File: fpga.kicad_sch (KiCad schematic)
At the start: 62 parts, among them CON1 SD_Card_DM3BT, P10 CONN_01X01, P11 CONN_01X01, P12 CONN_01X01, P13 CONN_01X01, P14 CONN_01X01, P15 CONN_01X01, P16 CONN_01X01, P3 CONN_02X04, P4 CONN_02X04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

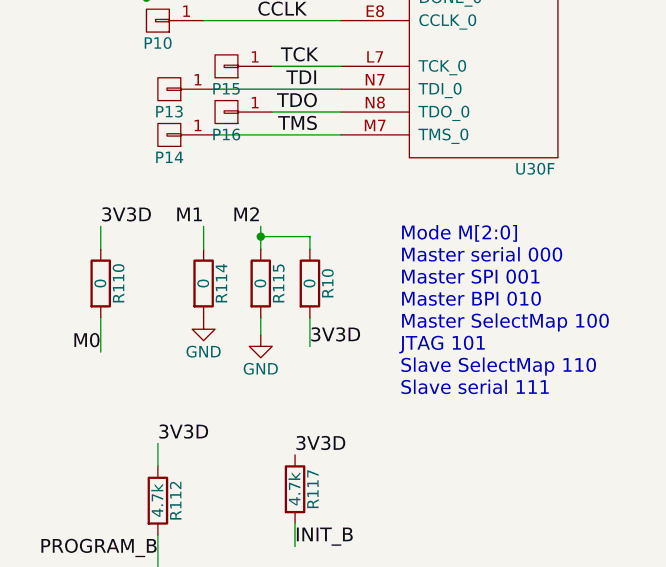
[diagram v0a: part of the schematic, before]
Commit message: Artix 7 Mode pin 2 was connected to 3.3 and Gnd. It is corrected. It is in JTAG mode for now. I will add dip switch
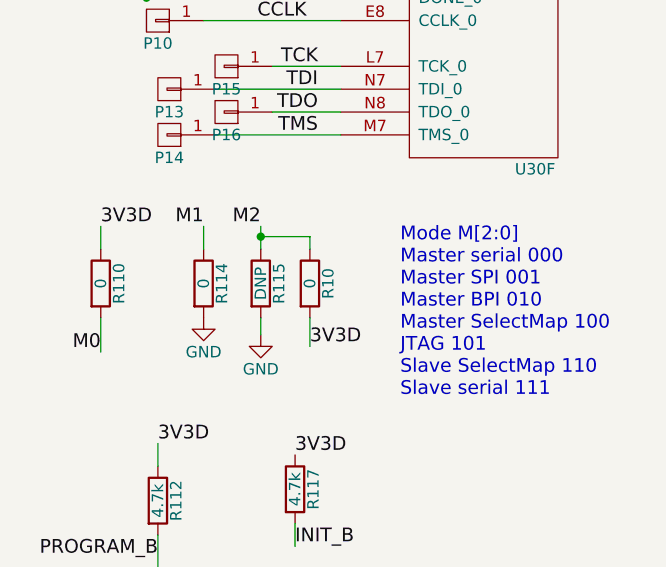
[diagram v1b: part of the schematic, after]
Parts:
- R115: value 0 -> DNP
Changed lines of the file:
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@@
 			)
 		)
-		(property "Value" "0"
+		(property "Value" "DNP"
 			(at 36.83 182.88 90)
 			(effects

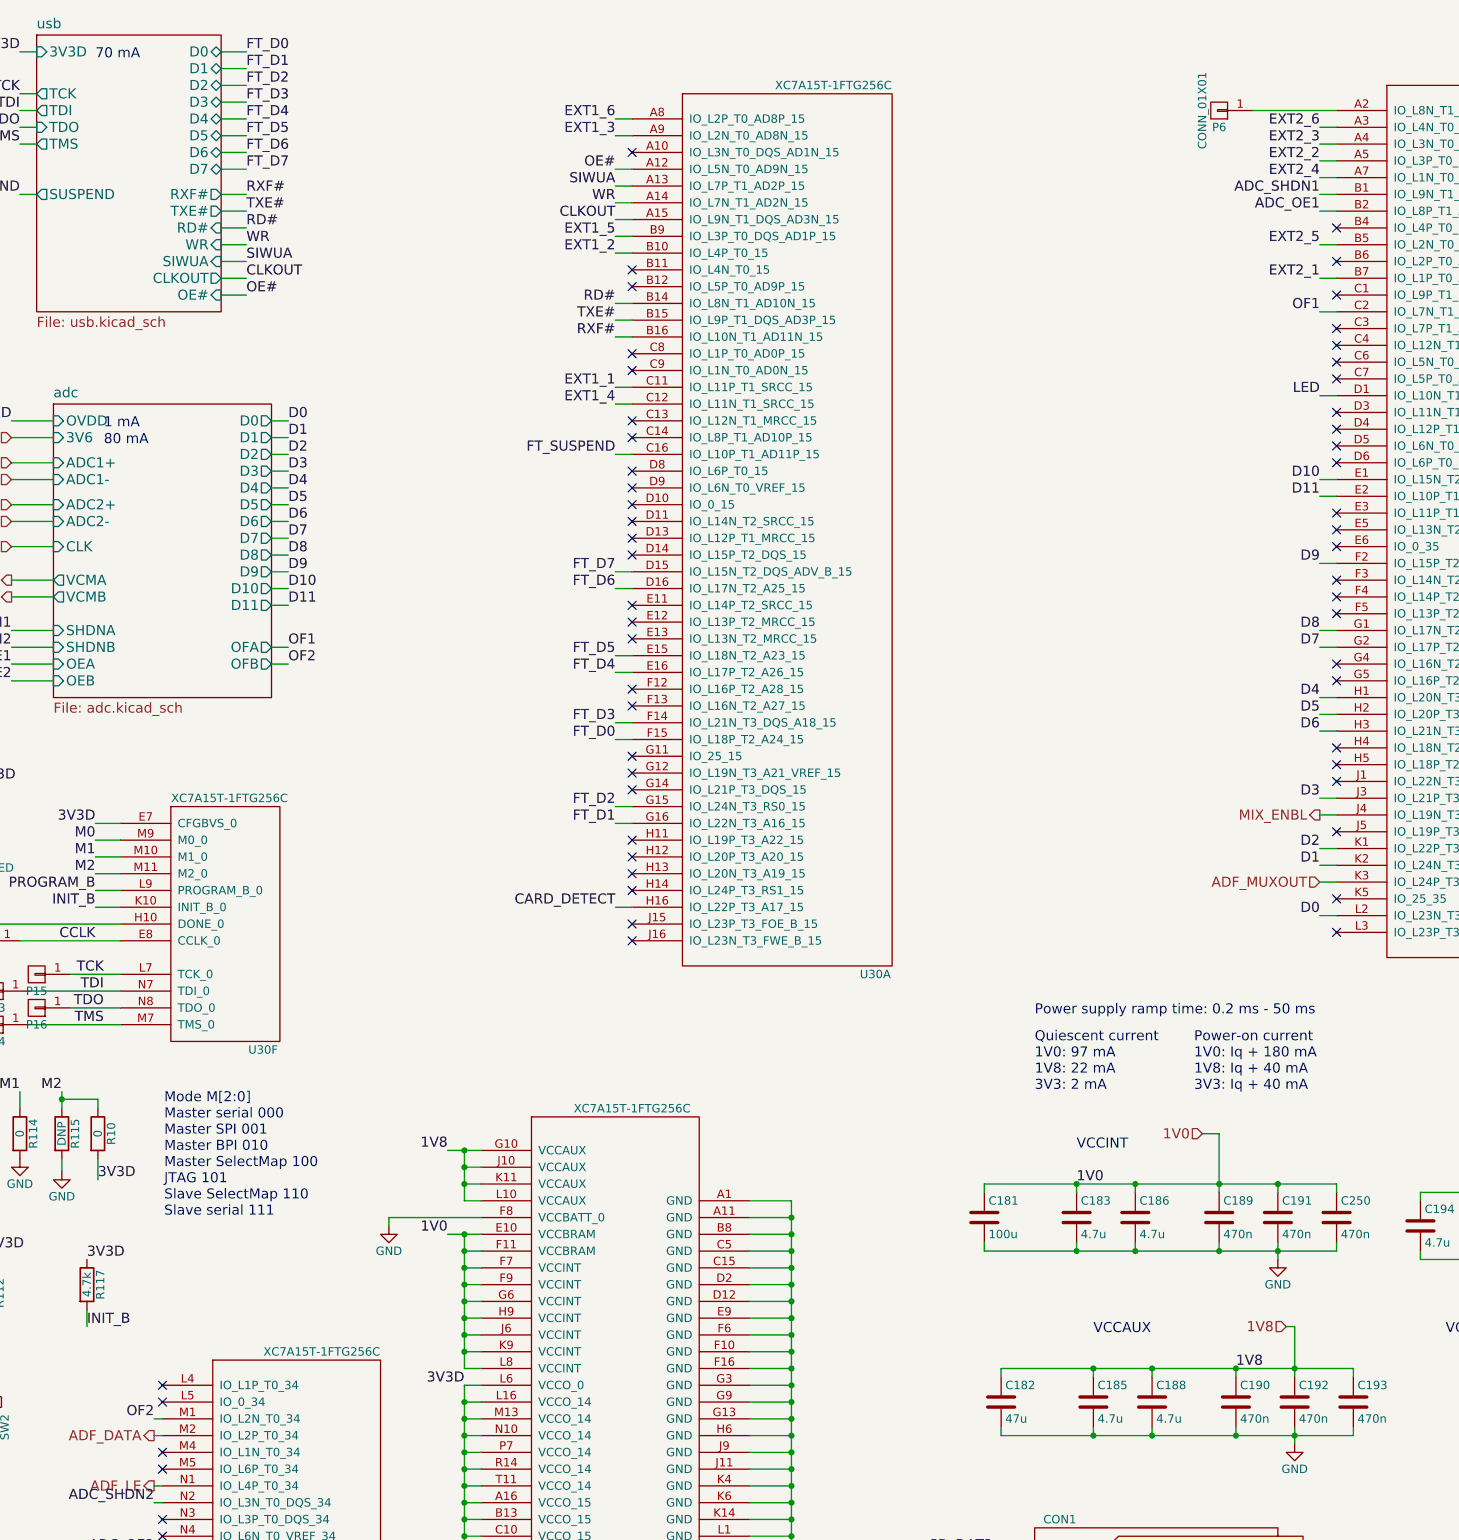
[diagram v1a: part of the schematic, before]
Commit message: Reset button is added. Detout is connected to an adc pin of fpga. Unused pad is deleted. Pins are check. Notes are added on pcb side. No problem related error drc excluded
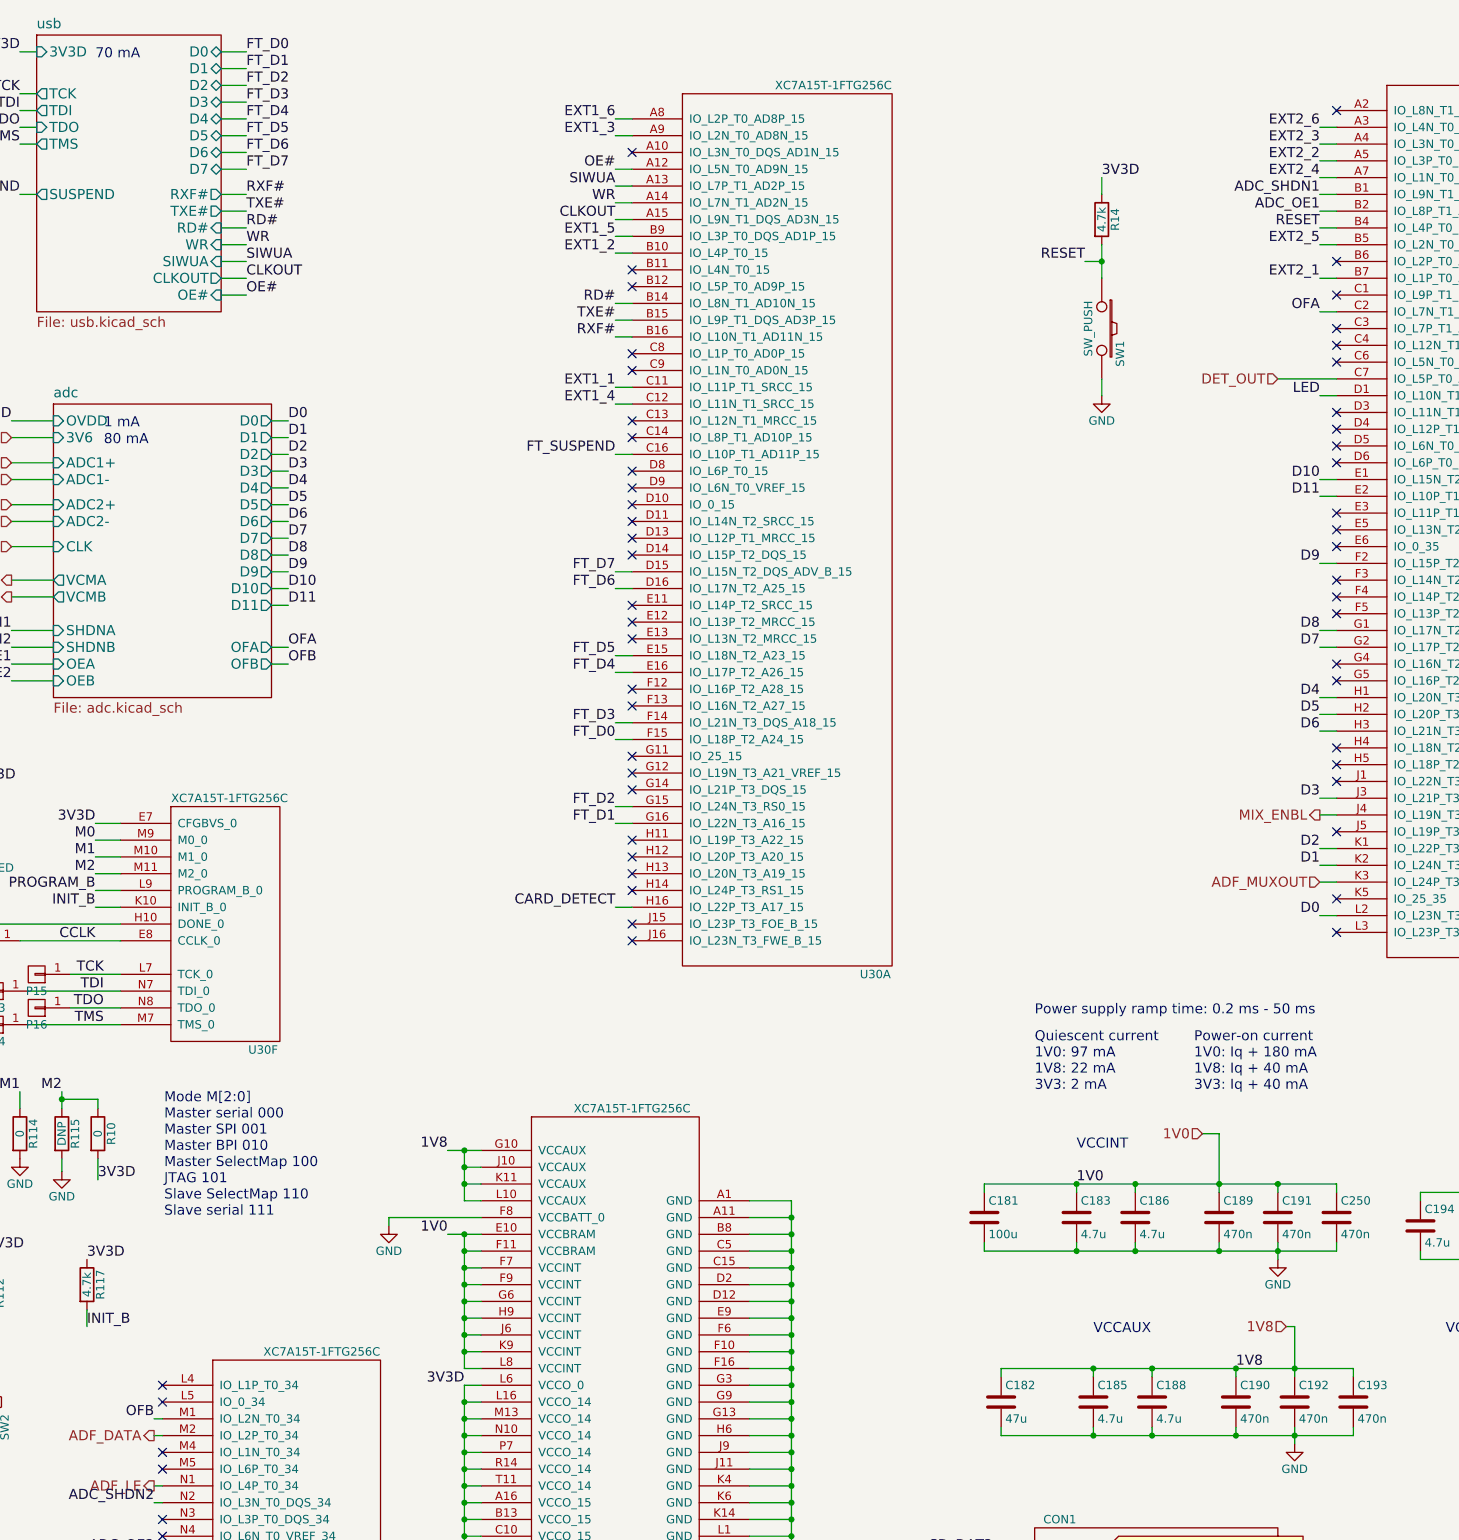
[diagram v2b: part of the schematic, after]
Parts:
- removed P6: CONN_01X01, fmcw3:TP_1.00, symbol fmcw3-rescue:CONN_01X01
- added R14: 4.7k, Footprints:SMD_0402, symbol fmcw3-rescue:R
- added SW1: SW_PUSH, fmcw3:EVP-AWBA2A, symbol fmcw3-rescue:SW_PUSH
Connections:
- net 3V3D: now also R14.1
- net GND: now also SW1.2
- net RESET: now reaches U30.B4 (IO_L4P_T0_35)
- net RESET: now also R14.2, SW1.1
- net DET_OUT: now reaches U30.C7 (IO_L5P_T0_AD13P_35)
- net OF1 renamed OFA
- net OF2 renamed OFB
- no-connect marks 102 -> 101

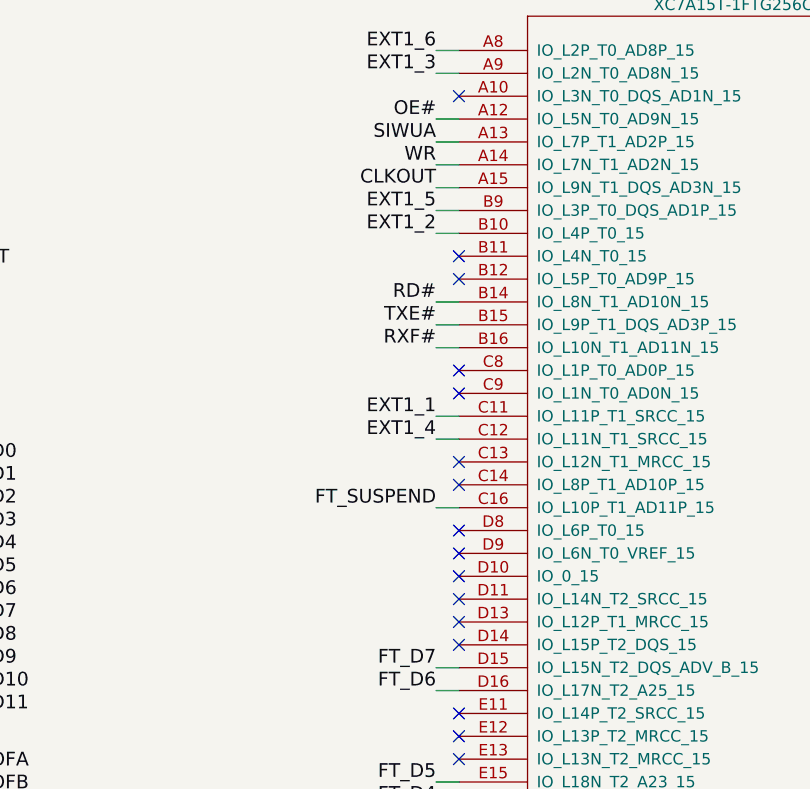
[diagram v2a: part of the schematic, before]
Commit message: fpga usb clkout pin and one more pin is changed
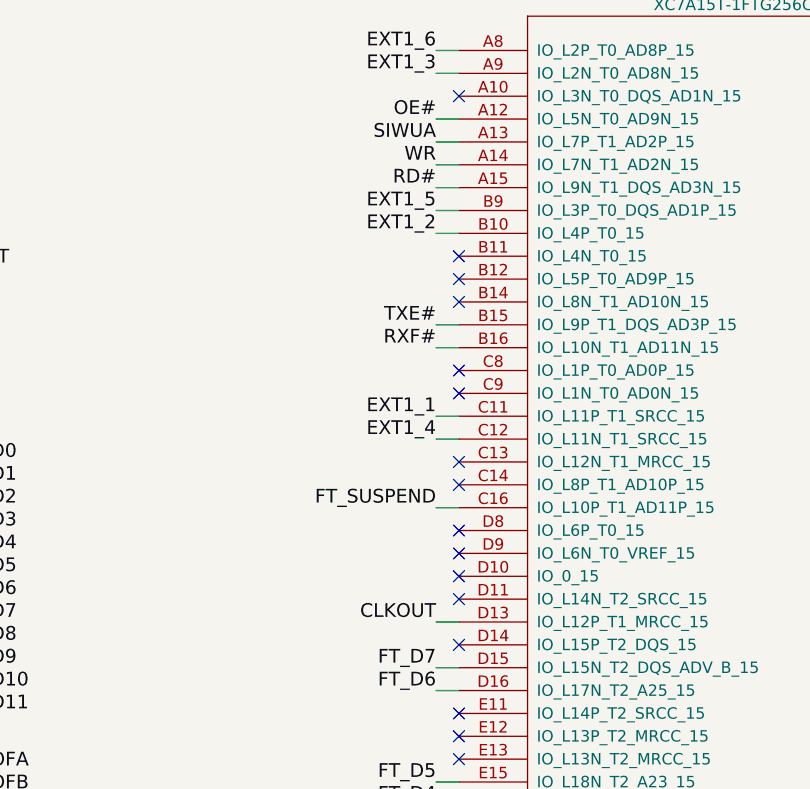
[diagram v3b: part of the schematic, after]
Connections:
- net CLKOUT: now also U30.D13 (IO_L12P_T1_MRCC_15); no longer U30.A15 (IO_L9N_T1_DQS_AD3N_15)
- net RD#: now also U30.A15 (IO_L9N_T1_DQS_AD3N_15); no longer U30.B14 (IO_L8N_T1_AD10N_15)
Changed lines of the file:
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@@
 	)
 	(no_connect
-		(at 123.19 92.71)
-	)
-	(no_connect
 		(at 229.87 60.96)
 	)
@@
 	)
 	(no_connect
+		(at 123.19 57.15)
+	)
+	(no_connect
 		(at 123.19 115.57)
 	)
@@
 	(wire
 		(pts
+			(xy 120.65 44.45) (xy 123.19 44.45)
+		)
+		(stroke
+			(width 0)
+			(type default)
+		)
+	)
+	(wire
+		(pts
 			(xy 97.79 246.38) (xy 97.79 248.92)
 		)
@@
 	(wire
 		(pts
-			(xy 120.65 57.15) (xy 123.19 57.15)
-		)
-		(stroke
-			(width 0)
-			(type default)
-		)
-	)
-	(wire
-		(pts
 			(xy 71.12 95.25) (xy 68.58 95.25)
 		)
@@
 	(wire
 		(pts
+			(xy 120.65 92.71) (xy 123.19 92.71)
+		)
+		(stroke
+			(width 0)
+			(type default)
+		)
+	)
+	(wire
+		(pts
 			(xy 97.79 266.7) (xy 100.33 266.7)
 		)
@@
 	(wire
 		(pts
-			(xy 123.19 44.45) (xy 120.65 44.45)
-		)
-		(stroke
-			(width 0)
-			(type default)
-		)
-	)
-	(wire
-		(pts
 			(xy 86.36 195.58) (xy 100.33 195.58)
 		)
@@
 		)
 	)
-	(label "CLKOUT"
-		(at 120.65 44.45 180)
-		(effects
-			(font
-				(size 1.524 1.524)
-			)
-			(justify right bottom)
-		)
-	)
 	(label "D8"
 		(at 71.12 95.25 0)
@@
 	)
 	(label "RD#"
-		(at 120.65 57.15 180)
+		(at 120.65 44.45 180)
 		(effects
 			(font
@@
 		(effects
 			(font
+				(size 1.524 1.524)
+			)
+			(justify right bottom)
+		)
+	)
+	(label "CLKOUT"
+		(at 120.65 92.71 180)
+		(effects
+			(font

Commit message: I increased the gap between voltage pours and also corrected signals cutting copper pour. Also not connected gnd occured in some layers are corrected with no copper zoens
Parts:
- R10: value 0 -> DNP
- R115: value DNP -> 0
- U30: value XC7A15T-1FTG256C -> XC7A35T-1FTG256C
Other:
- sheet adc ports: added 3V8; removed 3V6
- note added: "in SPI Flash mode, JTAG can be used."
- moved on the sheet: R10, R110, R112, R114, R115, R117, SW2
